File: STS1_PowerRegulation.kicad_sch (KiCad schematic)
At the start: 28 parts, among them U24 MCP1725-3302E_MC, U3 MCP1725-3302E_MC

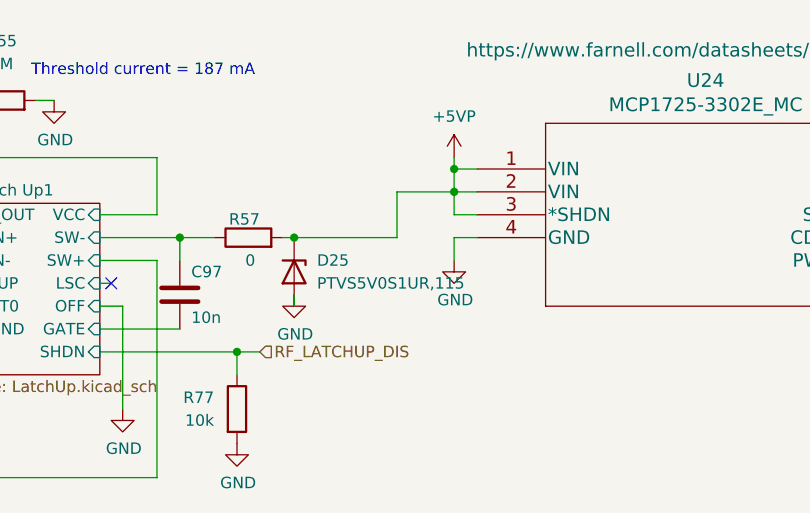
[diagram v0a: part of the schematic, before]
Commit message: Update kicad files to v9.0 from v6.0
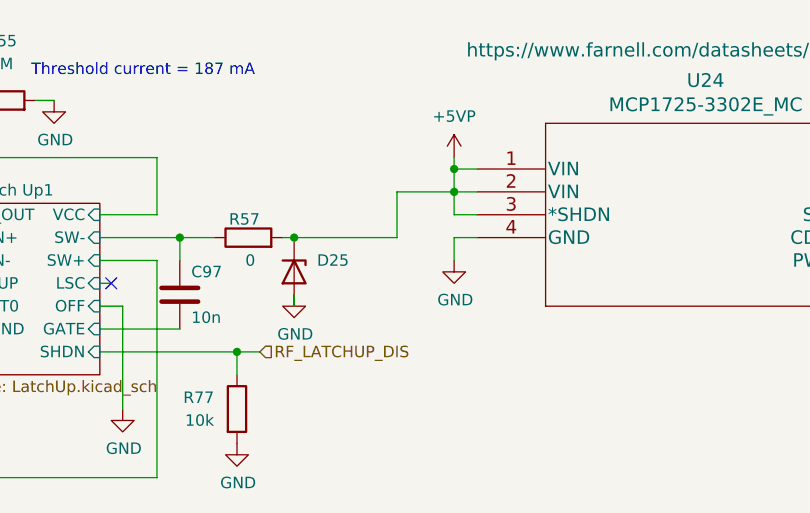
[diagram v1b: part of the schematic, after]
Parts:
- D24: value PTVS5V0S1UR,115 -> PTVS5V0S1UR,115

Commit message: Increase the value of R54 from 220K to 1M to reduce the STM latch-up protection threshold to ~190 mA
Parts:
- R54: value 220k -> 1M; JLCPCB Part # C4285297 -> (none); Manufacturer_Part_Number ERJ-H3EF5102V -> MR06X1004FTL
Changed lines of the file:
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@@
 			)
 		)
-		(property "Value" "220k"
+		(property "Value" "1M"
 			(at 106.68 28.956 90)
 			(effects
@@
 			)
 		)
-		(property "JLCPCB Part #" "C4285297"
+		(property "JLCPCB Part #" ""
 			(at 106.68 33.02 0)
 			(effects
@@
 			)
 		)
-		(property "Manufacturer_Part_Number" "ERJ-H3EF5102V"
+		(property "Manufacturer_Part_Number" "MR06X1004FTL "
 			(at 106.68 33.02 0)
 			(effects
